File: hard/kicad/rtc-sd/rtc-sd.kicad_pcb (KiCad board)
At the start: 2 copper layers, 53.3 x 130.8 mm, 38 parts, among them J1 SIDECAR, J2 SD0, J3 SD1, J4 SPI2, J5 SPI3, J6 RTC, J7 EXPANSION, Q1 2N7000, U1 74HC138, U2 74HC174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

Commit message: minor IC placement
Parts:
- moved U1 2.54 mm to (68.6, 88.9)
- moved U2 1.27 mm to (68.6, 64.8)
- moved U3 1.27 mm to (45.7, 64.8)
- moved U4 1.27 mm to (57.1, 64.8)
- moved U6 1.27 mm to (68.6, 36.8)
- moved D4 0.63 mm to (54.6, 59.1)
- moved D5 0.63 mm to (52.1, 59.1)
- moved R6 0.63 mm to (58.4, 59.1)
- moved R7 0.63 mm to (48.3, 59.1)
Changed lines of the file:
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@@
 	(footprint "Diode_THT:D_DO-35_SOD27_P2.54mm_Vertical_AnodeUp"
 		(layer "F.Cu")
-		(at 54.61 59.69 90)
+		(at 54.61 59.055 90)
 		(descr "Diode, DO-35_SOD27 series, Axial, Vertical, pin pitch=2.54mm, , length*diameter=4*2mm^2, , http://www.diodes.com/_files/packages/DO-35.pdf")
 		(tags "Diode DO-35_SOD27 series Axial Vertical pin pitch 2.54mm  length 4mm diameter 2mm")
@@
 	(footprint "Resistor_THT:R_Axial_DIN0207_L6.3mm_D2.5mm_P2.54mm_Vertical"
 		(layer "F.Cu")
-		(at 58.42 59.69 90)
+		(at 58.42 59.055 90)
 		(descr "Resistor, Axial_DIN0207 series, Axial, Vertical, pin pitch=2.54mm, 0.25W = 1/4W, length*diameter=6.3*2.5mm^2, http://cdn-reichelt.de/documents/datenblatt/B400/1_4W%23YAG.pdf")
 		(tags "Resistor Axial_DIN0207 series Axial Vertical pin pitch 2.54mm 0.25W = 1/4W length 6.3mm diameter 2.5mm")
@@
 	(footprint "Package_DIP:DIP-20_W7.62mm_Socket"
 		(layer "F.Cu")
-		(at 68.58 38.1)
+		(at 68.58 36.83)
 		(descr "20-lead though-hole mounted DIP package, row spacing 7.62 mm (300 mils), Socket")
 		(tags "THT DIP DIL PDIP 2.54mm 7.62mm 300mil Socket")
@@
 	(footprint "Diode_THT:D_DO-35_SOD27_P2.54mm_Vertical_AnodeUp"
 		(layer "F.Cu")
-		(at 52.07 59.69 90)
+		(at 52.07 59.055 90)
 		(descr "Diode, DO-35_SOD27 series, Axial, Vertical, pin pitch=2.54mm, , length*diameter=4*2mm^2, , http://www.diodes.com/_files/packages/DO-35.pdf")
 		(tags "Diode DO-35_SOD27 series Axial Vertical pin pitch 2.54mm  length 4mm diameter 2mm")
@@
 	(footprint "Package_DIP:DIP-16_W7.62mm_Socket"
 		(layer "F.Cu")
-		(at 57.15 66.04)
+		(at 57.15 64.77)
 		(descr "16-lead though-hole mounted DIP package, row spacing 7.62 mm (300 mils), Socket")
 		(tags "THT DIP DIL PDIP 2.54mm 7.62mm 300mil Socket")
@@
 	(footprint "Package_DIP:DIP-16_W7.62mm_Socket"
 		(layer "F.Cu")
-		(at 45.72 66.04)
+		(at 45.72 64.77)
 		(descr "16-lead though-hole mounted DIP package, row spacing 7.62 mm (300 mils), Socket")
 		(tags "THT DIP DIL PDIP 2.54mm 7.62mm 300mil Socket")
@@
 	(footprint "Package_DIP:DIP-16_W7.62mm_Socket"
 		(layer "F.Cu")
-		(at 68.58 91.44)
+		(at 68.58 88.9)
 		(descr "16-lead though-hole mounted DIP package, row spacing 7.62 mm (300 mils), Socket")
 		(tags "THT DIP DIL PDIP 2.54mm 7.62mm 300mil Socket")
@@
 	(footprint "Package_DIP:DIP-16_W7.62mm_Socket"
 		(layer "F.Cu")
-		(at 68.58 66.04)
+		(at 68.58 64.77)
 		(descr "16-lead though-hole mounted DIP package, row spacing 7.62 mm (300 mils), Socket")
 		(tags "THT DIP DIL PDIP 2.54mm 7.62mm 300mil Socket")
@@
 	(footprint "Resistor_THT:R_Axial_DIN0207_L6.3mm_D2.5mm_P2.54mm_Vertical"
 		(layer "F.Cu")
-		(at 48.26 59.69 90)
+		(at 48.26 59.055 90)
 		(descr "Resistor, Axial_DIN0207 series, Axial, Vertical, pin pitch=2.54mm, 0.25W = 1/4W, length*diameter=6.3*2.5mm^2, http://cdn-reichelt.de/documents/datenblatt/B400/1_4W%23YAG.pdf")
 		(tags "Resistor Axial_DIN0207 series Axial Vertical pin pitch 2.54mm 0.25W = 1/4W length 6.3mm diameter 2.5mm")

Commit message: minor passive repositioning
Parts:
- moved C2 7.99 mm to (33.7, 61.0)
- moved R8 2.54 mm to (35.6, 106.7), turned to 90 degrees
- moved R2 2.54 mm to (29.2, 63.5)
- moved R9 2.54 mm to (35.6, 100.3), turned to 90 degrees
- moved D5 1.27 mm to (50.8, 59.1)
- moved R1 1.05 mm to (39.6, 61.0), turned to 0 degrees
- moved R6 0.64 mm to (57.8, 59.1)
- moved R7 0.63 mm to (47.6, 59.1)
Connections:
- R1 pad 1: +5V -> /~{SCLK}
- R1 pad 2: /~{SCLK} -> +5V
- R8 pad 1: +5V -> /SD0
- R8 pad 2: /SD0 -> +5V
- R9 pad 1: +5V -> /SD1
- R9 pad 2: /SD1 -> +5V
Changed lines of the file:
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@@
 		)
 		(property "Value" "BAT85"
-			(at -2.54 0.635 0)
+			(at -2.54 0 0)
 			(unlocked yes)
 			(layer "F.SilkS")
@@
 	(footprint "Capacitor_THT:C_Disc_D3.8mm_W2.6mm_P2.50mm"
 		(layer "F.Cu")
-		(at 26.67 64.77)
+		(at 33.695 60.96)
 		(descr "C, Disc series, Radial, pin pitch=2.50mm, , diameter*width=3.8*2.6mm^2, Capacitor, http://www.vishay.com/docs/45233/krseries.pdf")
 		(tags "C Disc series Radial pin pitch 2.50mm  diameter 3.8mm width 2.6mm Capacitor")
 		(property "Reference" "C2"
-			(at 4.445 0 0)
+			(at 1.23 -1.42 0)
 			(unlocked yes)
 			(layer "B.SilkS")
@@
 		)
 		(property "Value" "68p"
-			(at 5.08 -1.27 0)
+			(at 1.23 -2.54 0)
 			(layer "F.SilkS")
 			(effects
@@
 	(footprint "Resistor_THT:R_Axial_DIN0207_L6.3mm_D2.5mm_P2.54mm_Vertical"
 		(layer "F.Cu")
-		(at 40.64 60.96 180)
+		(at 39.595 60.96)
 		(descr "Resistor, Axial_DIN0207 series, Axial, Vertical, pin pitch=2.54mm, 0.25W = 1/4W, length*diameter=6.3*2.5mm^2, http://cdn-reichelt.de/documents/datenblatt/B400/1_4W%23YAG.pdf")
 		(tags "Resistor Axial_DIN0207 series Axial Vertical pin pitch 2.54mm 0.25W = 1/4W length 6.3mm diameter 2.5mm")
 		(property "Reference" "R1"
-			(at -1.905 0 0)
+			(at 1.27 -1.27 0)
 			(unlocked yes)
 			(layer "B.SilkS")
@@
 		)
 		(property "Value" "1K2"
-			(at -3.175 0 0)
+			(at 1.27 -2.54 0)
 			(layer "F.SilkS")
 			(effects
@@
 		)
 		(property "Footprint" "Resistor_THT:R_Axial_DIN0207_L6.3mm_D2.5mm_P2.54mm_Vertical"
-			(at 0 0 180)
+			(at 0 0 0)
 			(unlocked yes)
 			(layer "F.Fab")
@@
 		)
 		(property "Datasheet" ""
-			(at 0 0 180)
+			(at 0 0 0)
 			(unlocked yes)
 			(layer "F.Fab")
@@
 		)
 		(property "Description" ""
-			(at 0 0 180)
+			(at 0 0 0)
 			(unlocked yes)
 			(layer "F.Fab")
@@
 		)
 		(fp_line
-			(start 3.59 1.5)
-			(end 3.59 -1.5)
+			(start -1.5 -1.5)
+			(end -1.5 1.5)
 			(stroke
 				(width 0.05)
@@
 		)
 		(fp_line
-			(start 3.59 -1.5)
-			(end -1.5 -1.5)
+			(start -1.5 1.5)
+			(end 3.59 1.5)
 			(stroke
 				(width 0.05)
@@
 		)
 		(fp_line
-			(start -1.5 1.5)
-			(end 3.59 1.5)
+			(start 3.59 -1.5)
+			(end -1.5 -1.5)
 			(stroke
 				(width 0.05)
@@
 		)
 		(fp_line
-			(start -1.5 -1.5)
-			(end -1.5 1.5)
+			(start 3.59 1.5)
+			(end 3.59 -1.5)
 			(stroke
 				(width 0.05)
@@
 		)
 		(pad "1" thru_hole circle
-			(at 0 0 180)
+			(at 0 0)
 			(size 1.6 1.6)
 			(drill 0.8)
 			(layers "*.Cu" "*.Mask")
 			(remove_unused_layers no)
-			(net 2 "+5V")
+			(net 8 "/~{SCLK}")
 			(pintype "passive")
 		)
 		(pad "2" thru_hole oval
-			(at 2.54 0 180)
+			(at 2.54 0)
 			(size 1.6 1.6)
 			(drill 0.8)
 			(layers "*.Cu" "*.Mask")
 			(remove_unused_layers no)
-			(net 8 "/~{SCLK}")
+			(net 2 "+5V")
 			(pintype "passive")
 		)
@@
 	(footprint "Resistor_THT:R_Axial_DIN0207_L6.3mm_D2.5mm_P2.54mm_Vertical"
 		(layer "F.Cu")
-		(at 29.21 60.96 180)
+		(at 29.21 63.5 180)
 		(descr "Resistor, Axial_DIN0207 series, Axial, Vertical, pin pitch=2.54mm, 0.25W = 1/4W, length*diameter=6.3*2.5mm^2, http://cdn-reichelt.de/documents/datenblatt/B400/1_4W%23YAG.pdf")
 		(tags "Resistor Axial_DIN0207 series Axial Vertical pin pitch 2.54mm 0.25W = 1/4W length 6.3mm diameter 2.5mm")
@@
 		)
 		(property "Value" "3K3"
-			(at -3.175 0 0)
+			(at 0 -2.54 0)
 			(layer "F.SilkS")
 			(effects
@@
 	(footprint "Resistor_THT:R_Axial_DIN0207_L6.3mm_D2.5mm_P2.54mm_Vertical"
 		(layer "F.Cu")
-		(at 35.56 97.79 -90)
+		(at 35.56 100.33 90)
 		(descr "Resistor, Axial_DIN0207 series, Axial, Vertical, pin pitch=2.54mm, 0.25W = 1/4W, length*diameter=6.3*2.5mm^2, http://cdn-reichelt.de/documents/datenblatt/B400/1_4W%23YAG.pdf")
 		(tags "Resistor Axial_DIN0207 series Axial Vertical pin pitch 2.54mm 0.25W = 1/4W length 6.3mm diameter 2.5mm")
 		(property "Reference" "R9"
-			(at 0 -1.905 0)
+			(at 0 1.905 0)
 			(unlocked yes)
 			(layer "B.SilkS")
@@
 		)
 		(property "Value" "3K3"
-			(at 1.27 -3.175 0)
+			(at 0 3.175 0)
 			(unlocked yes)
 			(layer "F.SilkS")
@@
 		)
 		(property "Footprint" "Resistor_THT:R_Axial_DIN0207_L6.3mm_D2.5mm_P2.54mm_Vertical"
-			(at 0 0 -90)
+			(at 0 0 90)
 			(unlocked yes)
 			(layer "F.Fab")
@@
 		)
 		(property "Datasheet" ""
-			(at 0 0 -90)
+			(at 0 0 90)
 			(unlocked yes)
 			(layer "F.Fab")
@@
 		)
 		(property "Description" ""
-			(at 0 0 -90)
+			(at 0 0 90)
 			(unlocked yes)
 			(layer "F.Fab")
@@
 		)
 		(fp_line
-			(start -1.5 1.5)
-			(end 3.59 1.5)
+			(start 3.59 -1.5)
+			(end -1.5 -1.5)
 			(stroke
 				(width 0.05)
@@
 		)
 		(fp_line
-			(start 3.59 1.5)
-			(end 3.59 -1.5)
+			(start -1.5 -1.5)
+			(end -1.5 1.5)
 			(stroke
 				(width 0.05)
@@
 		)
 		(fp_line
-			(start -1.5 -1.5)
-			(end -1.5 1.5)
+			(start 3.59 1.5)
+			(end 3.59 -1.5)
 			(stroke
 				(width 0.05)
@@
 		)
 		(fp_line
-			(start 3.59 -1.5)
-			(end -1.5 -1.5)
+			(start -1.5 1.5)
+			(end 3.59 1.5)
 			(stroke
 				(width 0.05)
@@
 		)
 		(pad "1" thru_hole circle
-			(at 0 0 270)
+			(at 0 0 90)
 			(size 1.6 1.6)
 			(drill 0.8)
 			(layers "*.Cu" "*.Mask")
 			(remove_unused_layers no)
-			(net 2 "+5V")
+			(net 16 "/SD1")
 			(pintype "passive")
 		)
 		(pad "2" thru_hole oval
-			(at 2.54 0 270)
+			(at 2.54 0 90)
 			(size 1.6 1.6)
 			(drill 0.8)
 			(layers "*.Cu" "*.Mask")
 			(remove_unused_layers no)
-			(net 16 "/SD1")
+			(net 2 "+5V")
 			(pintype "passive")
 		)
@@
 	(footprint "Resistor_THT:R_Axial_DIN0207_L6.3mm_D2.5mm_P2.54mm_Vertical"
 		(layer "F.Cu")
-		(at 35.56 104.14 -90)
+		(at 35.56 106.68 90)
 		(descr "Resistor, Axial_DIN0207 series, Axial, Vertical, pin pitch=2.54mm, 0.25W = 1/4W, length*diameter=6.3*2.5mm^2, http://cdn-reichelt.de/documents/datenblatt/B400/1_4W%23YAG.pdf")
 		(tags "Resistor Axial_DIN0207 series Axial Vertical pin pitch 2.54mm 0.25W = 1/4W length 6.3mm diameter 2.5mm")
 		(property "Reference" "R8"
-			(at 0 -1.905 0)
+			(at 0 1.905 0)
 			(unlocked yes)
 			(layer "B.SilkS")
@@
 		)
 		(property "Value" "3K3"
-			(at 1.27 -3.175 0)
+			(at 0 3.175 0)
 			(unlocked yes)
 			(layer "F.SilkS")
@@
 		)
 		(property "Footprint" "Resistor_THT:R_Axial_DIN0207_L6.3mm_D2.5mm_P2.54mm_Vertical"
-			(at 0 0 -90)
+			(at 0 0 90)
 			(unlocked yes)
 			(layer "F.Fab")
@@
 		)
 		(property "Datasheet" ""
-			(at 0 0 -90)
+			(at 0 0 90)
 			(unlocked yes)
 			(layer "F.Fab")
@@
 		)
 		(property "Description" ""
-			(at 0 0 -90)
+			(at 0 0 90)
 			(unlocked yes)
 			(layer "F.Fab")
@@
 		)
 		(fp_line
-			(start -1.5 1.5)
-			(end 3.59 1.5)
+			(start 3.59 -1.5)
+			(end -1.5 -1.5)
 			(stroke
 				(width 0.05)
@@
 		)
 		(fp_line
-			(start 3.59 1.5)
-			(end 3.59 -1.5)
+			(start -1.5 -1.5)
+			(end -1.5 1.5)
 			(stroke
 				(width 0.05)
@@
 		)
 		(fp_line
-			(start -1.5 -1.5)
-			(end -1.5 1.5)
+			(start 3.59 1.5)
+			(end 3.59 -1.5)
 			(stroke
 				(width 0.05)
@@
 		)
 		(fp_line
-			(start 3.59 -1.5)
-			(end -1.5 -1.5)
+			(start -1.5 1.5)
+			(end 3.59 1.5)
 			(stroke
 				(width 0.05)
@@
 		)
 		(pad "1" thru_hole circle
-			(at 0 0 270)
+			(at 0 0 90)
 			(size 1.6 1.6)
 			(drill 0.8)
 			(layers "*.Cu" "*.Mask")
 			(remove_unused_layers no)
-			(net 2 "+5V")
+			(net 14 "/SD0")
 			(pintype "passive")
 		)
 		(pad "2" thru_hole oval
-			(at 2.54 0 270)
+			(at 2.54 0 90)
 			(size 1.6 1.6)
 			(drill 0.8)
 			(layers "*.Cu" "*.Mask")
 			(remove_unused_layers no)
-			(net 14 "/SD0")
+			(net 2 "+5V")
 			(pintype "passive")
 		)
@@
 	(footprint "Resistor_THT:R_Axial_DIN0207_L6.3mm_D2.5mm_P2.54mm_Vertical"
 		(layer "F.Cu")
-		(at 58.42 59.055 90)
+		(at 57.785 59.055 90)
 		(descr "Resistor, Axial_DIN0207 series, Axial, Vertical, pin pitch=2.54mm, 0.25W = 1/4W, length*diameter=6.3*2.5mm^2, http://cdn-reichelt.de/documents/datenblatt/B400/1_4W%23YAG.pdf")
 		(tags "Resistor Axial_DIN0207 series Axial Vertical pin pitch 2.54mm 0.25W = 1/4W length 6.3mm diameter 2.5mm")
@@
 	(footprint "Diode_THT:D_DO-35_SOD27_P2.54mm_Vertical_AnodeUp"
 		(layer "F.Cu")
-		(at 52.07 59.055 90)
+		(at 50.8 59.055 90)
 		(descr "Diode, DO-35_SOD27 series, Axial, Vertical, pin pitch=2.54mm, , length*diameter=4*2mm^2, , http://www.diodes.com/_files/packages/DO-35.pdf")
 		(tags "Diode DO-35_SOD27 series Axial Vertical pin pitch 2.54mm  length 4mm diameter 2mm")
@@
 		)
 		(property "Value" "BAT85"
-			(at -2.54 -0.635 0)
+			(at -2.54 0 0)
 			(unlocked yes)
 			(layer "F.SilkS")
@@
 	(footprint "Resistor_THT:R_Axial_DIN0207_L6.3mm_D2.5mm_P2.54mm_Vertical"
 		(layer "F.Cu")
-		(at 48.26 59.055 90)
+		(at 47.625 59.055 90)
 		(descr "Resistor, Axial_DIN0207 series, Axial, Vertical, pin pitch=2.54mm, 0.25W = 1/4W, length*diameter=6.3*2.5mm^2, http://cdn-reichelt.de/documents/datenblatt/B400/1_4W%23YAG.pdf")
 		(tags "Resistor Axial_DIN0207 series Axial Vertical pin pitch 2.54mm 0.25W = 1/4W length 6.3mm diameter 2.5mm")

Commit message: sidecar mostly routed
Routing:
- net GND: track 0.00 -> 462.3 mm
- net +5V: track 0.00 -> 269.8 mm, vias 0 -> 1
- net /~{CS0}: track 0.00 -> 124.7 mm, vias 0 -> 2
- net /CLK: track 0.00 -> 123.5 mm, vias 0 -> 4
- net PD2: track 0.00 -> 108.7 mm, vias 0 -> 4
- net PD0: track 0.00 -> 108.1 mm, vias 0 -> 2
- net PD1: track 0.00 -> 107.3 mm, vias 0 -> 4
- net /~{CS1}: track 0.00 -> 106.9 mm, vias 0 -> 1
- net /BR~{W}: track 0.00 -> 98.7 mm, vias 0 -> 2
- net /~{IOX}: track 0.00 -> 92.6 mm, vias 0 -> 2
- net PD7: track 0.00 -> 88.0 mm, vias 0 -> 1
- net PD6: track 0.00 -> 88.0 mm, vias 0 -> 1
- net /~{CS2}: track 0.00 -> 83.6 mm, vias 0 -> 3
- net /BA0: track 0.00 -> 81.1 mm, vias 0 -> 2
- net /BA1: track 0.00 -> 81.1 mm, vias 0 -> 2
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- added copper zone on B.Cu, net +5V
- added copper zone on F.Cu, net GND

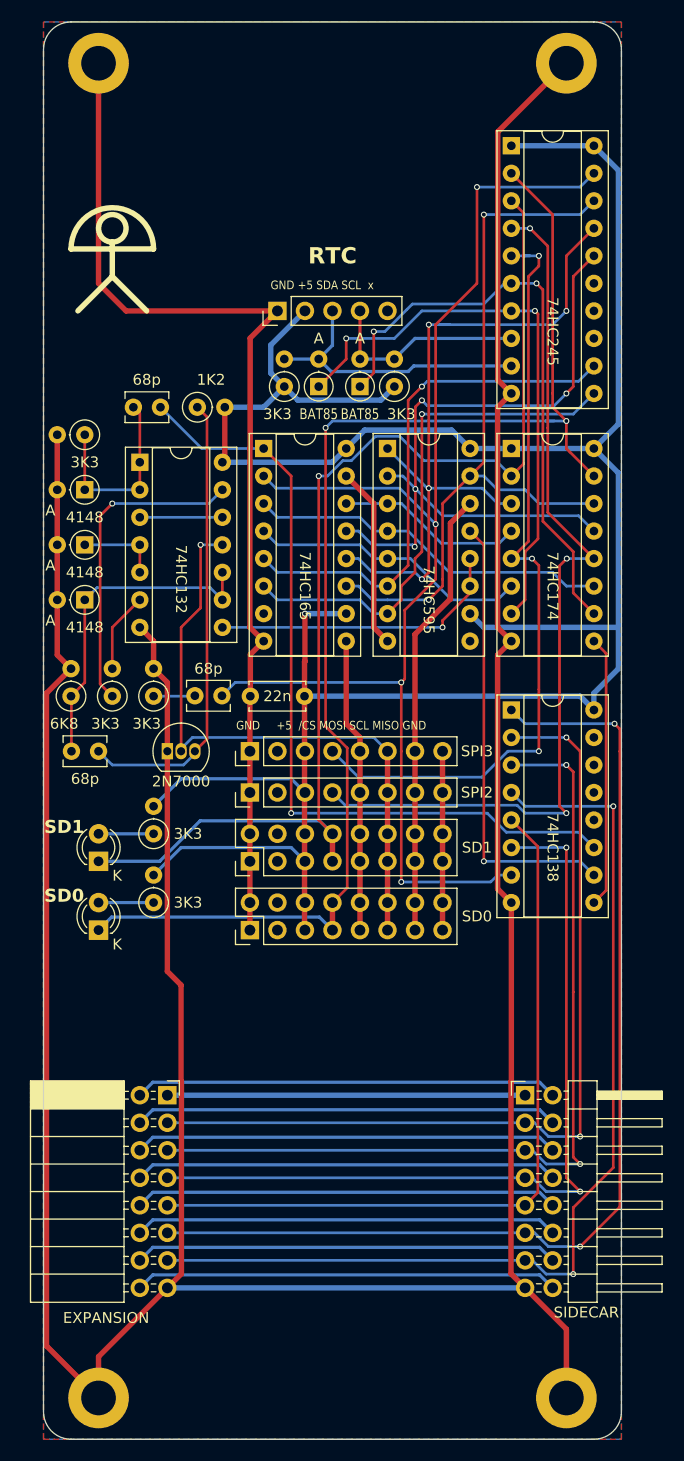
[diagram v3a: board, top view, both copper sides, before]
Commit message: sidecar fully routed
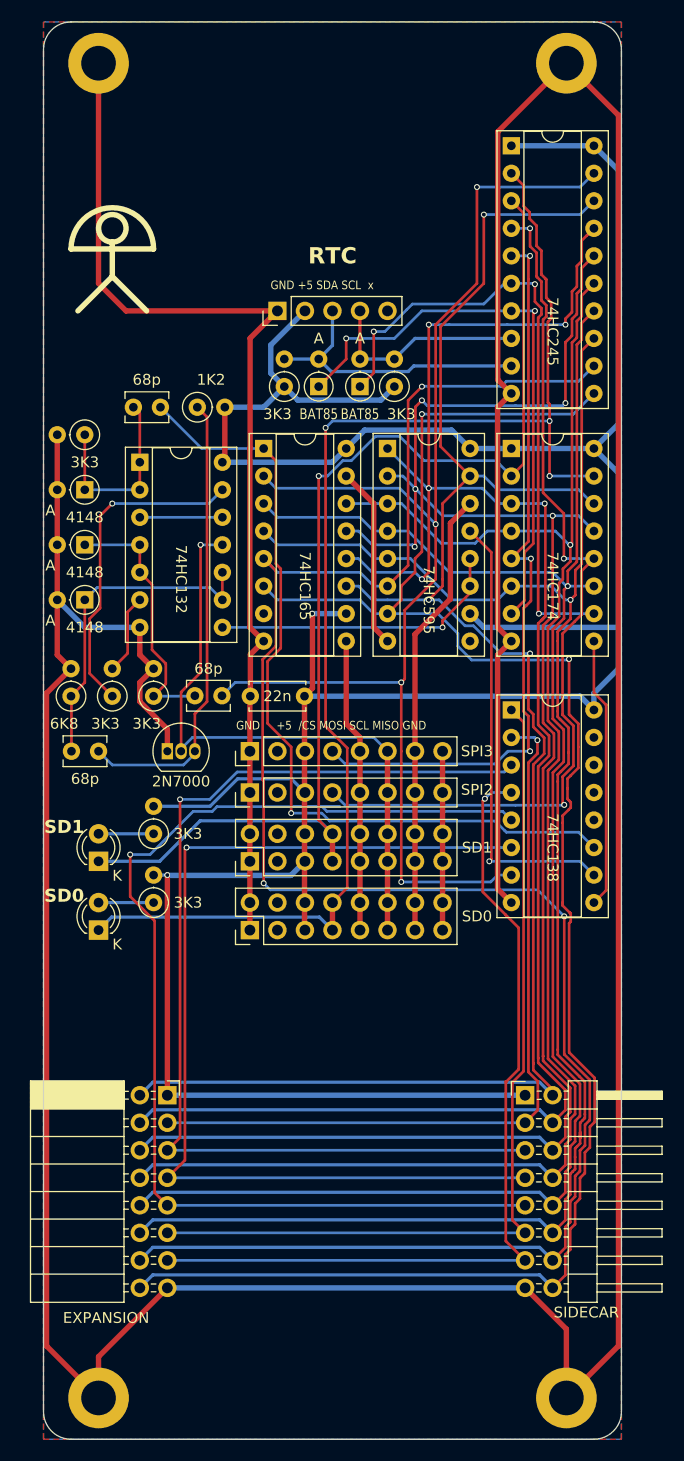
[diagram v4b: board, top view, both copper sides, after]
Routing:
- net PD6: track 88.0 -> 182.1 mm, vias 1 -> 3
- net PD5: track 65.1 -> 159.1 mm, vias 0 -> 1
- net PD3: track 56.3 -> 149.3 mm, vias 0 -> 1
- net PD4: track 72.7 -> 159.8 mm, vias 0 -> 1
- net PD7: track 88.0 -> 169.5 mm, vias 1 -> 2
- net PD1: track 107.3 -> 170.3 mm, vias 4 -> 5
- net PD2: track 108.7 -> 170.7 mm, vias 4 -> 5
- net PD0: track 108.1 -> 164.3 mm, vias 2 -> 3
- net GND: track 462.3 -> 512.5 mm
- net /BA3: track 70.1 -> 113.3 mm, vias 0 -> 1
- net +5V: track 269.8 -> 288.7 mm, vias 1 -> 2
- net /BA2: track 76.0 -> 94.2 mm, vias 2 -> 1
- net /BA1: track 81.1 -> 97.8 mm, vias 2 -> 1
- net /BR~{W}: track 98.7 -> 82.7 mm, vias 2 -> 0
- net /D_CLK: track 11.4 -> 24.3 mm
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
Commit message: add some silkscreen to RTC/SD sidecar
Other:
- board text added: "2024.11"
- board text added: "@zuiko21"
- board text added: "DS1307"
- board text added: "FastSPI + RTC"
- board text added: "SD Card module"
- board text added: "v1"
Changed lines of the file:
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@@
 		)
 		(property "Value" "SIDECAR"
-			(at 5.655 20.05 0)
+			(at 2.54 21.59 0)
 			(layer "F.SilkS")
 			(effects
@@
 		)
 		(property "Value" "EXPANSION"
-			(at -5.65 20.55 0)
+			(at -3.81 21.59 0)
 			(layer "F.SilkS")
 			(effects
@@
 	)
 	(gr_arc
-		(start 27.94 46.355)
-		(mid 31.75 42.545)
-		(end 35.56 46.355)
+		(start 26.67 115.57)
+		(mid 30.48 111.76)
+		(end 34.29 115.57)
 		(stroke
 			(width 0.5)
@@
 	)
 	(gr_line
-		(start 31.75 48.895)
-		(end 34.925 52.07)
+		(start 30.48 118.11)
+		(end 33.655 121.285)
 		(stroke
 			(width 0.5)
@@
 	)
 	(gr_line
-		(start 31.75 48.895)
-		(end 28.575 52.07)
+		(start 30.48 118.11)
+		(end 27.305 121.285)
 		(stroke
 			(width 0.5)
@@
 	)
 	(gr_line
-		(start 31.75 45.72)
-		(end 31.75 48.895)
+		(start 30.48 114.935)
+		(end 30.48 118.11)
 		(stroke
 			(width 0.5)
@@
 	)
 	(gr_line
-		(start 27.94 46.355)
-		(end 35.56 46.355)
+		(start 26.67 115.57)
+		(end 34.29 115.57)
 		(stroke
 			(width 0.5)
@@
 	)
 	(gr_circle
-		(center 31.75 44.45)
-		(end 33.02 44.45)
+		(center 30.48 113.665)
+		(end 31.75 113.665)
 		(stroke
 			(width 0.5)
@@
 		(layer "Edge.Cuts")
 	)
+	(gr_text "FastSPI\n+\nRTC"
+		(at 32.385 47.625 0)
+		(layer "F.SilkS")
+		(effects
+			(font
+				(size 2.5 2.5)
+				(thickness 0.5)
+				(bold yes)
+			)
+			(justify bottom)
+		)
+	)
+	(gr_text "SD Card module"
+		(at 43.815 113.665 0)
+		(layer "F.SilkS")
+		(effects
+			(font
+				(size 1.5 1.5)
+				(thickness 0.3)
+				(bold yes)
+			)
+			(justify left bottom)
+		)
+	)
 	(gr_text "A"
 		(at 26.035 80.645 0)
@@
 		)
 	)
+	(gr_text "DS1307"
+		(at 47.625 45.085 0)
+		(layer "F.SilkS")
+		(effects
+			(font
+				(size 1.5 1.5)
+				(thickness 0.3)
+				(bold yes)
+			)
+			(justify left bottom)
+		)
+	)
 	(gr_text "GND     +5  /CS MOSI SCL MISO GND  "
 		(at 43.18 90.805 0)
@@
 		)
 	)
+	(gr_text "@zuiko21"
+		(at 33.655 55.88 0)
+		(layer "F.SilkS")
+		(effects
+			(font
+				(size 2 2)
+				(thickness 0.4)
+				(bold yes)
+			)
+			(justify bottom)
+		)
+	)
+	(gr_text "2024.11"
+		(at 67.25 34.925 0)
+		(layer "F.SilkS")
+		(effects
+			(font
+				(size 1.5 1.5)
+				(thickness 0.3)
+				(bold yes)
+			)
+			(justify left bottom)
+		)
+	)
+	(gr_text "v1"
+		(at 38.735 30.48 0)
+		(layer "F.SilkS")
+		(effects
+			(font
+				(size 2 2)
+				(thickness 0.4)
+				(bold yes)
+			)
+			(justify right bottom)
+		)
+	)
